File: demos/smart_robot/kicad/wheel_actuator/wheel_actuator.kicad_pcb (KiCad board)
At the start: 95 x 55 mm, 9 parts, among them M1 WHEEL_MOTOR_DESIGN_ENVELOPE, U1 AT32M416, U2 DRV8323, U3 TCAN3413DR

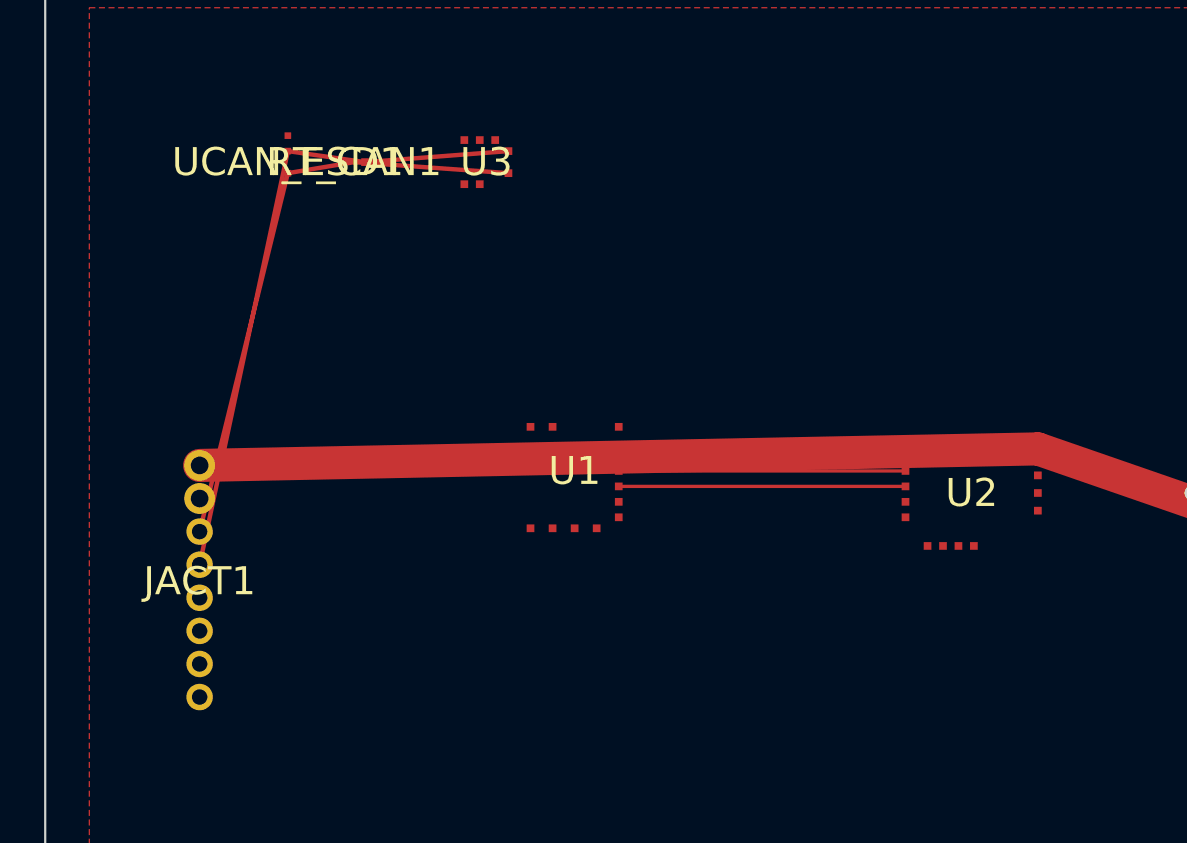
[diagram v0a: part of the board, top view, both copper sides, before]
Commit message: Validate wheel CAN placement from PCB import
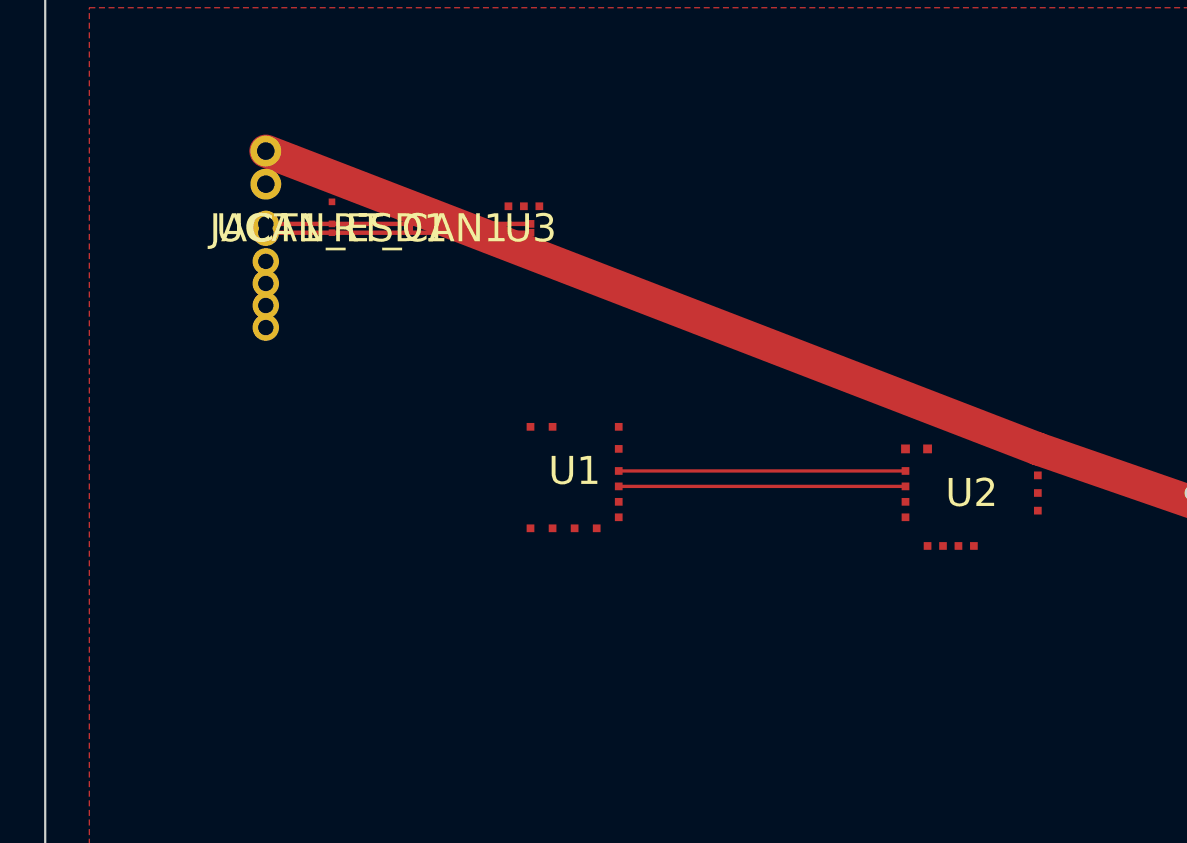
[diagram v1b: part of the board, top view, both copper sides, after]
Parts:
- moved JACT1 16.3 mm to (10.0, 12.0)
- moved RT_CAN1 4.24 mm to (17.0, 12.0)
- moved U3 3.61 mm to (22.0, 12.0)
- moved UCAN_ESD1 3.61 mm to (13.0, 12.0)
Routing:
- net robot_canl: track 29.2 -> 12.0 mm
- net robot_canh: track 26.8 -> 12.0 mm
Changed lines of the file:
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@@
     (pad "SOC" smd rect (at 3 0.8) (size 0.35 0.35) (layers "F.Cu" "F.Paste" "F.Mask") (net 23 "cur_w")))
   (footprint "CircuitCI:TCAN3413" (layer "F.Cu")
-    (at 20 9 0)
+    (at 22 12 0)
     (property "Reference" "U3" (at 0 0 0) (layer "F.SilkS"))
     (property "Value" "TCAN3413DR" (at 0 1 0) (layer "F.Fab"))
@@
     (pad "TXD" smd rect (at -1 1) (size 0.35 0.35) (layers "F.Cu" "F.Paste" "F.Mask") (net 5 "wheel_can_tx"))
     (pad "RXD" smd rect (at -0.3 1) (size 0.35 0.35) (layers "F.Cu" "F.Paste" "F.Mask") (net 6 "wheel_can_rx"))
-    (pad "CANH" smd rect (at 1 0.5) (size 0.35 0.35) (layers "F.Cu" "F.Paste" "F.Mask") (net 7 "robot_canh"))
-    (pad "CANL" smd rect (at 1 -0.5) (size 0.35 0.35) (layers "F.Cu" "F.Paste" "F.Mask") (net 8 "robot_canl")))
+    (pad "CANH" smd rect (at 0 -0.2) (size 0.35 0.35) (layers "F.Cu" "F.Paste" "F.Mask") (net 7 "robot_canh"))
+    (pad "CANL" smd rect (at 0 0.2) (size 0.35 0.35) (layers "F.Cu" "F.Paste" "F.Mask") (net 8 "robot_canl")))
   (footprint "CircuitCI:ESD2CAN24_Q1" (layer "F.Cu")
-    (at 11 9 0)
+    (at 13 12 0)
     (property "Reference" "UCAN_ESD1" (at 0 0 0) (layer "F.SilkS"))
     (property "Value" "ESD2CAN24-Q1" (at 0 1 0) (layer "F.Fab"))
     (fp_rect (start -1 -1) (end 1 1) (stroke (width 0.05) (type solid)) (fill none) (layer "F.Fab"))
-    (pad "CANH" smd rect (at 0 0.5) (size 0.3 0.3) (layers "F.Cu" "F.Paste" "F.Mask") (net 7 "robot_canh"))
-    (pad "CANL" smd rect (at 0 -0.5) (size 0.3 0.3) (layers "F.Cu" "F.Paste" "F.Mask") (net 8 "robot_canl"))
+    (pad "CANH" smd rect (at 0 -0.2) (size 0.3 0.3) (layers "F.Cu" "F.Paste" "F.Mask") (net 7 "robot_canh"))
+    (pad "CANL" smd rect (at 0 0.2) (size 0.3 0.3) (layers "F.Cu" "F.Paste" "F.Mask") (net 8 "robot_canl"))
     (pad "GND" smd rect (at 0 -1.2) (size 0.3 0.3) (layers "F.Cu" "F.Paste" "F.Mask") (net 2 "gnd")))
   (footprint "CircuitCI:CAN_Termination" (layer "F.Cu")
-    (at 14 9 0)
+    (at 17 12 0)
     (property "Reference" "RT_CAN1" (at 0 0 0) (layer "F.SilkS"))
     (property "Value" "120R" (at 0 1 0) (layer "F.Fab"))
@@
     (pad "PHASE_W" smd rect (at -1.5 1) (size 1.0 1.0) (layers "F.Cu" "F.Paste" "F.Mask") (net 32 "phase_w")))
   (footprint "CircuitCI:JST_VH_8Pin_Actuator_Bus" (layer "F.Cu")
-    (at 7 28 0)
+    (at 10 12 0)
     (property "Reference" "JACT1" (at 0 0 0) (layer "F.SilkS"))
     (property "Value" "B8P-VH_ACTUATOR_BUS" (at 0 1 0) (layer "F.Fab"))
     (fp_rect (start -2 -8) (end 2 8) (stroke (width 0.05) (type solid)) (fill none) (layer "F.Fab"))
-    (pad "VBAT" thru_hole oval (at 0 -5.25) (size 1.4 1.4) (drill 0.8) (layers "*.Cu" "*.Mask") (net 1 "vwheel_sw"))
-    (pad "GND" thru_hole oval (at 0 -3.75) (size 1.4 1.4) (drill 0.8) (layers "*.Cu" "*.Mask") (net 2 "gnd"))
-    (pad "CANH" thru_hole oval (at 0 -2.25) (size 1.2 1.2) (drill 0.7) (layers "*.Cu" "*.Mask") (net 7 "robot_canh"))
-    (pad "CANL" thru_hole oval (at 0 -0.75) (size 1.2 1.2) (drill 0.7) (layers "*.Cu" "*.Mask") (net 8 "robot_canl"))
-    (pad "AUX_5V" thru_hole oval (at 0 0.75) (size 1.2 1.2) (drill 0.7) (layers "*.Cu" "*.Mask") (net 4 "5v_aux"))
-    (pad "ENABLE" thru_hole oval (at 0 2.25) (size 1.2 1.2) (drill 0.7) (layers "*.Cu" "*.Mask") (net 27 "enable_in"))
-    (pad "FAULT" thru_hole oval (at 0 3.75) (size 1.2 1.2) (drill 0.7) (layers "*.Cu" "*.Mask") (net 28 "fault_out"))
-    (pad "SYNC" thru_hole oval (at 0 5.25) (size 1.2 1.2) (drill 0.7) (layers "*.Cu" "*.Mask") (net 29 "sync_in")))
-  (segment (start 7 25.75) (end 11 9.5) (width 0.20) (layer "F.Cu") (net 7))
-  (segment (start 11 9.5) (end 14 9.0) (width 0.20) (layer "F.Cu") (net 7))
-  (segment (start 14 9.0) (end 21 9.5) (width 0.20) (layer "F.Cu") (net 7))
-  (segment (start 7 27.25) (end 11 8.5) (width 0.20) (layer "F.Cu") (net 8))
-  (segment (start 11 8.5) (end 14.5 9.0) (width 0.20) (layer "F.Cu") (net 8))
-  (segment (start 14.5 9.0) (end 21 8.5) (width 0.20) (layer "F.Cu") (net 8))
-  (segment (start 7 22.75) (end 45 22.0) (width 1.50) (layer "F.Cu") (net 1))
+    (pad "VBAT" thru_hole oval (at 0 -3.5) (size 1.4 1.4) (drill 0.8) (layers "*.Cu" "*.Mask") (net 1 "vwheel_sw"))
+    (pad "GND" thru_hole oval (at 0 -2.0) (size 1.4 1.4) (drill 0.8) (layers "*.Cu" "*.Mask") (net 2 "gnd"))
+    (pad "CANH" thru_hole oval (at 0 -0.2) (size 1.2 1.2) (drill 0.7) (layers "*.Cu" "*.Mask") (net 7 "robot_canh"))
+    (pad "CANL" thru_hole oval (at 0 0.2) (size 1.2 1.2) (drill 0.7) (layers "*.Cu" "*.Mask") (net 8 "robot_canl"))
+    (pad "AUX_5V" thru_hole oval (at 0 1.5) (size 1.2 1.2) (drill 0.7) (layers "*.Cu" "*.Mask") (net 4 "5v_aux"))
+    (pad "ENABLE" thru_hole oval (at 0 2.5) (size 1.2 1.2) (drill 0.7) (layers "*.Cu" "*.Mask") (net 27 "enable_in"))
+    (pad "FAULT" thru_hole oval (at 0 3.5) (size 1.2 1.2) (drill 0.7) (layers "*.Cu" "*.Mask") (net 28 "fault_out"))
+    (pad "SYNC" thru_hole oval (at 0 4.5) (size 1.2 1.2) (drill 0.7) (layers "*.Cu" "*.Mask") (net 29 "sync_in")))
+  (segment (start 10 11.8) (end 13 11.8) (width 0.20) (layer "F.Cu") (net 7))
+  (segment (start 13 11.8) (end 17 11.8) (width 0.20) (layer "F.Cu") (net 7))
+  (segment (start 17 11.8) (end 22 11.8) (width 0.20) (layer "F.Cu") (net 7))
+  (segment (start 10 12.2) (end 13 12.2) (width 0.20) (layer "F.Cu") (net 8))
+  (segment (start 13 12.2) (end 17 12.2) (width 0.20) (layer "F.Cu") (net 8))
+  (segment (start 17 12.2) (end 22 12.2) (width 0.20) (layer "F.Cu") (net 8))
+  (segment (start 10 8.5) (end 45 22.0) (width 1.50) (layer "F.Cu") (net 1))
   (segment (start 45 22.0) (end 58 26.5) (width 1.50) (layer "F.Cu") (net 1))
   (segment (start 64 27.0) (end 81.5 28.0) (width 1.20) (layer "F.Cu") (net 30))

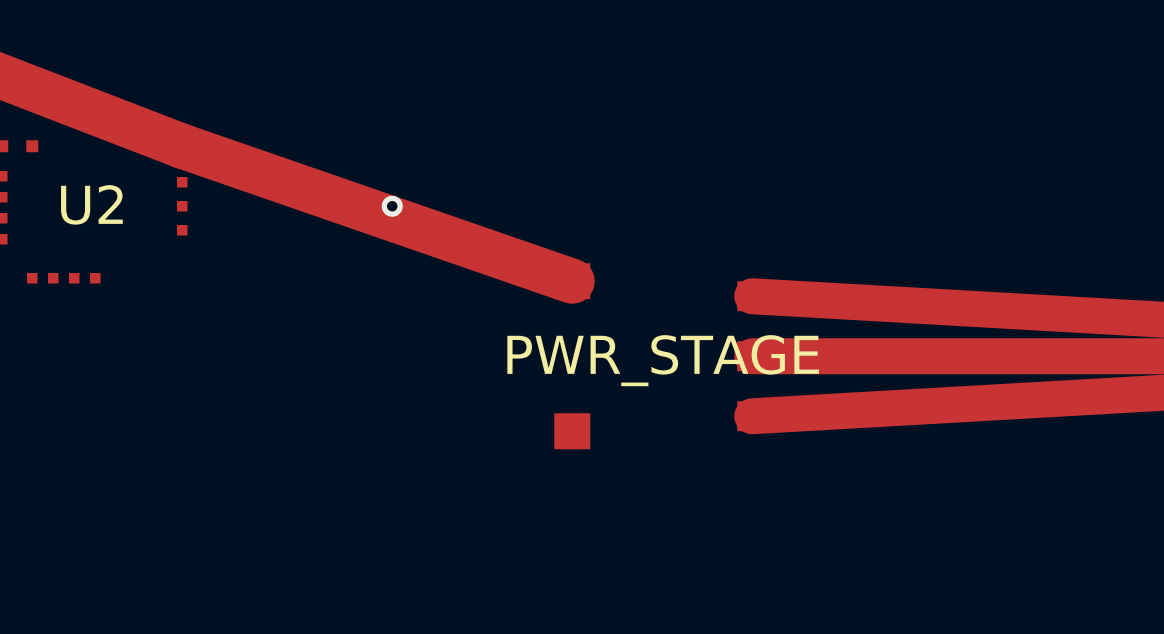
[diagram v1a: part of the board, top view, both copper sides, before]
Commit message: Validate wheel current sense placement
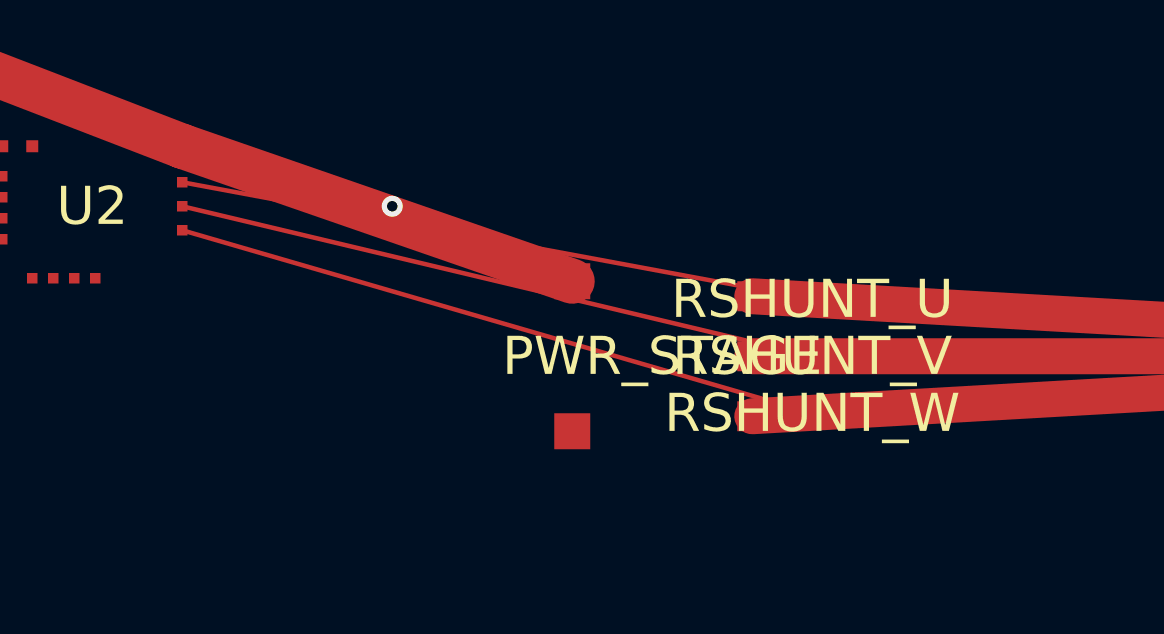
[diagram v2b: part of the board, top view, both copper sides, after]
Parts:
- added RSHUNT_U: 5mR_1W, CircuitCI:Phase_Shunt_5mR, F.Cu at (66.0, 27.1)
- added RSHUNT_V: 5mR_1W, CircuitCI:Phase_Shunt_5mR, F.Cu at (66.0, 29.0)
- added RSHUNT_W: 5mR_1W, CircuitCI:Phase_Shunt_5mR, F.Cu at (66.0, 30.9)
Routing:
- net cur_w: track 0.00 -> 21.9 mm
- net cur_v: track 0.00 -> 21.6 mm
- net cur_u: track 0.00 -> 21.4 mm
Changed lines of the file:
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@@
     (pad "PHASE_V" smd rect (at 3 0) (size 1.0 1.0) (layers "F.Cu" "F.Paste" "F.Mask") (net 31 "phase_v"))
     (pad "PHASE_W" smd rect (at 3 2) (size 1.0 1.0) (layers "F.Cu" "F.Paste" "F.Mask") (net 32 "phase_w")))
+  (footprint "CircuitCI:Phase_Shunt_5mR" (layer "F.Cu")
+    (at 66 27.1 0)
+    (property "Reference" "RSHUNT_U" (at 0 0 0) (layer "F.SilkS"))
+    (property "Value" "5mR_1W" (at 0 1 0) (layer "F.Fab"))
+    (fp_rect (start -0.9 -0.45) (end 0.9 0.45) (stroke (width 0.05) (type solid)) (fill none) (layer "F.Fab"))
+    (pad "A" smd rect (at -0.5 0) (size 0.45 0.45) (layers "F.Cu" "F.Paste" "F.Mask") (net 30 "phase_u"))
+    (pad "B" smd rect (at 0.5 0) (size 0.45 0.45) (layers "F.Cu" "F.Paste" "F.Mask") (net 21 "cur_u")))
+  (footprint "CircuitCI:Phase_Shunt_5mR" (layer "F.Cu")
+    (at 66 29 0)
+    (property "Reference" "RSHUNT_V" (at 0 0 0) (layer "F.SilkS"))
+    (property "Value" "5mR_1W" (at 0 1 0) (layer "F.Fab"))
+    (fp_rect (start -0.9 -0.45) (end 0.9 0.45) (stroke (width 0.05) (type solid)) (fill none) (layer "F.Fab"))
+    (pad "A" smd rect (at -0.5 0) (size 0.45 0.45) (layers "F.Cu" "F.Paste" "F.Mask") (net 31 "phase_v"))
+    (pad "B" smd rect (at 0.5 0) (size 0.45 0.45) (layers "F.Cu" "F.Paste" "F.Mask") (net 22 "cur_v")))
+  (footprint "CircuitCI:Phase_Shunt_5mR" (layer "F.Cu")
+    (at 66 30.9 0)
+    (property "Reference" "RSHUNT_W" (at 0 0 0) (layer "F.SilkS"))
+    (property "Value" "5mR_1W" (at 0 1 0) (layer "F.Fab"))
+    (fp_rect (start -0.9 -0.45) (end 0.9 0.45) (stroke (width 0.05) (type solid)) (fill none) (layer "F.Fab"))
+    (pad "A" smd rect (at -0.5 0) (size 0.45 0.45) (layers "F.Cu" "F.Paste" "F.Mask") (net 32 "phase_w"))
+    (pad "B" smd rect (at 0.5 0) (size 0.45 0.45) (layers "F.Cu" "F.Paste" "F.Mask") (net 23 "cur_w")))
   (footprint "CircuitCI:Wheel_Motor_Envelope" (layer "F.Cu")
     (at 83 29 0)
@@
   (segment (start 64 29.0) (end 81.5 29.0) (width 1.20) (layer "F.Cu") (net 31))
   (segment (start 64 31.0) (end 81.5 30.0) (width 1.20) (layer "F.Cu") (net 32))
+  (segment (start 66.0 27.1) (end 45 23.2) (width 0.15) (layer "F.Cu") (net 21))
+  (segment (start 66.0 29.0) (end 45 24.0) (width 0.15) (layer "F.Cu") (net 22))
+  (segment (start 66.0 30.9) (end 45 24.8) (width 0.15) (layer "F.Cu") (net 23))
   (segment (start 26 23.0) (end 39 23.0) (width 0.15) (layer "F.Cu") (net 9))
   (segment (start 26 23.7) (end 39 23.7) (width 0.15) (layer "F.Cu") (net 10))
